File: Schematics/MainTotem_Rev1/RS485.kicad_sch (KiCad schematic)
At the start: 0 parts

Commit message: Added RS485 functionality to MainTotemLite
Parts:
- added C23, C25: 0.1u, symbol Device:C
- added C24: 10u, symbol Device:C
- added C27, C32: 100n, symbol Device:C
- added D1: SM712_SOT23, Package_TO_SOT_SMD:SOT-23, symbol Diode:SM712_SOT23
- added J1, J2: S6B-XH-A, S6B-XH-A:JST_S6B-XH-A, symbol TotemBusMale:S6B-XH-A
- added J3: Conn_02x05_Odd_Even, symbol Connector_Generic:Conn_02x05_Odd_Even
- added JP1: Jumper_2_Open, symbol Jumper:Jumper_2_Open
- added PROG: GREEN, symbol Device:LED
- added R1: 120, symbol Device:R
- added R10, R8, R9: 1k, symbol Device:R
- added R2, R3, R7: 10k, symbol Device:R
- added RS485: YELLOW, symbol Device:LED
- added U3: THVD1450D, D0008A_N, symbol RS485Transceiver:THVD1450D
- added U4: STM32G071KBT6, LQFP-32, symbol STM32G0:STM32G071KBT6
- added UH_OH: RED, symbol Device:LED
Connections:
- new net: R8.1, U4.11 (PA4)
- new net: R9.1, U4.12 (PA5)
- new net: R10.1, U4.13 (PA6)
- new net: U3.4 (D), U4.19 (PA9)
- new net: R2.2, U3.1 (R), U4.21 (PA10)
- new net: R3.1, U3.2 (RE_N), U3.3 (DE), U4.23 (PA12[PA10])
- new net: J3.2 (Pin_2), U4.24 (PA13)
- new net: J3.4 (Pin_4), R7.1, U4.25 (PA14-BOOT0)
- new net: C27.1, J3.10 (Pin_10), U4.6 (PF2-NRST)
- new net: D1.1 (A1), J1.2, J2.2, JP1.2 (B), U3.6 (A)
- new net: D1.2 (A2), J1.3, J2.3, R1.2, U3.7 (B)
- new net: PROG.2 (A), R10.2
- new net: R8.2, UH_OH.2 (A)
- new net: R9.2, RS485.2 (A)
- new net: JP1.1 (A), R1.1
- new net +3V3: C23.1, C24.1, C25.1, C32.1, J1.1, J2.1, J3.1 (Pin_1), J3.6 (Pin_6), R2.1, U3.8 (VCC), U4.4 (VDD)
- new net BUSH7BOOT0: U4.27 (PB3)
- new net BUSH7NRST: U4.17 (PB2)
- new net BUSH7SWCLK: U4.16 (PB1)
- new net BUSH7SWDIO: U4.15 (PB0)
- new net BUSH7UARTRX: U4.32 (PB8)
- new net BUSHH7UARTTX: U4.1 (PB9)
- new net G0UARTRX: J3.8 (Pin_8), U4.10 (PA3)
- new net G0UARTTX: J3.7 (Pin_7), U4.9 (PA2)
- new net GND: C23.2, C24.2, C25.2, C27.2, C32.2, D1.3 (common), J1.4, J2.4, J3.3 (Pin_3), J3.5 (Pin_5), J3.9 (Pin_9), PROG.1 (K), R3.2, R7.2, RS485.1 (K), U3.5 (GND), U3.9 (PAD), U4.5 (VSS), UH_OH.1 (K)
- no-connect marks 0 -> 17
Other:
- note added: "Configure these as Analog Mode pins to avoid unwated signal"
- note added: "Don't connect the 3V3 unless you are powering the ShamanLink and other modules with it. It will compete with the 3V3 on the other boards. Also, you probably can't power the ShamanLink with it anyways since the PowerMUX expects inputs not only outputs."
- note added: "Label this jumper to determine if this MTL module is the terminating module on the RS485 bus"
- note added: "SWCLK/BOOT0, pull high to program with UART"
- note added: "SWDIO"

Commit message: Adding the MTL Schematics in post editing
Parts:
- added C64: 0.1u, symbol Device:C
- added D4: BAT54SW_115, BAT54SW_115:SOT65P210X110-3N, symbol BAT54SW_115:BAT54SW_115
- added SW2: SW_Push, symbol Switch:SW_Push
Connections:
- net +3V3: no longer C23.1, J1.1, J2.1
- net BUSH7NRST: now also D4.3, SW2.1; no longer U4.17 (PB2)
- net GND: now also C64.2, SW2.2
- new net: D4.2, U4.17 (PB2)
- new net 3V3PROGRAMMER: C23.1, C64.1, J1.1, J2.1
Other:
- note added: "I mean, this should be fine. The diode's forward voltage is about .32 V at the currents I am expecting. Therefore, if the G0 pulls to 0.1V LOW and the diode adds .32V, .42V must be less than .3Vdd for the NRST to register VIL. If Vdd is 3.3V, this shouldn't be an issue I hope."
- note added: "Pin PB2 needs to be set to OUTPUT OPEN DRAIN such that it never attempts to drive the net high. It resets the H7 by driving low, but if not driving, the pull up 10k resistor pulls up the net for us. If the G0 tries to drive the net high while the reset button is being pressed, there will be a 0 impedence short the gnd i.e. vcc to gnd :( The current could break the G0 or the H7, bad day. I placed 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"
- note added: "SL can power additional modules if they are not connected to power in order to program them"
- note removed: "Don't connect the 3V3 unless you are powering the ShamanLink and other modules with it. It will compete with the 3V3 on the other boards. Also, you probably can't power the ShamanLink with it anyways since the PowerMUX expects inputs not only outputs."
- moved on the sheet: C24, C25

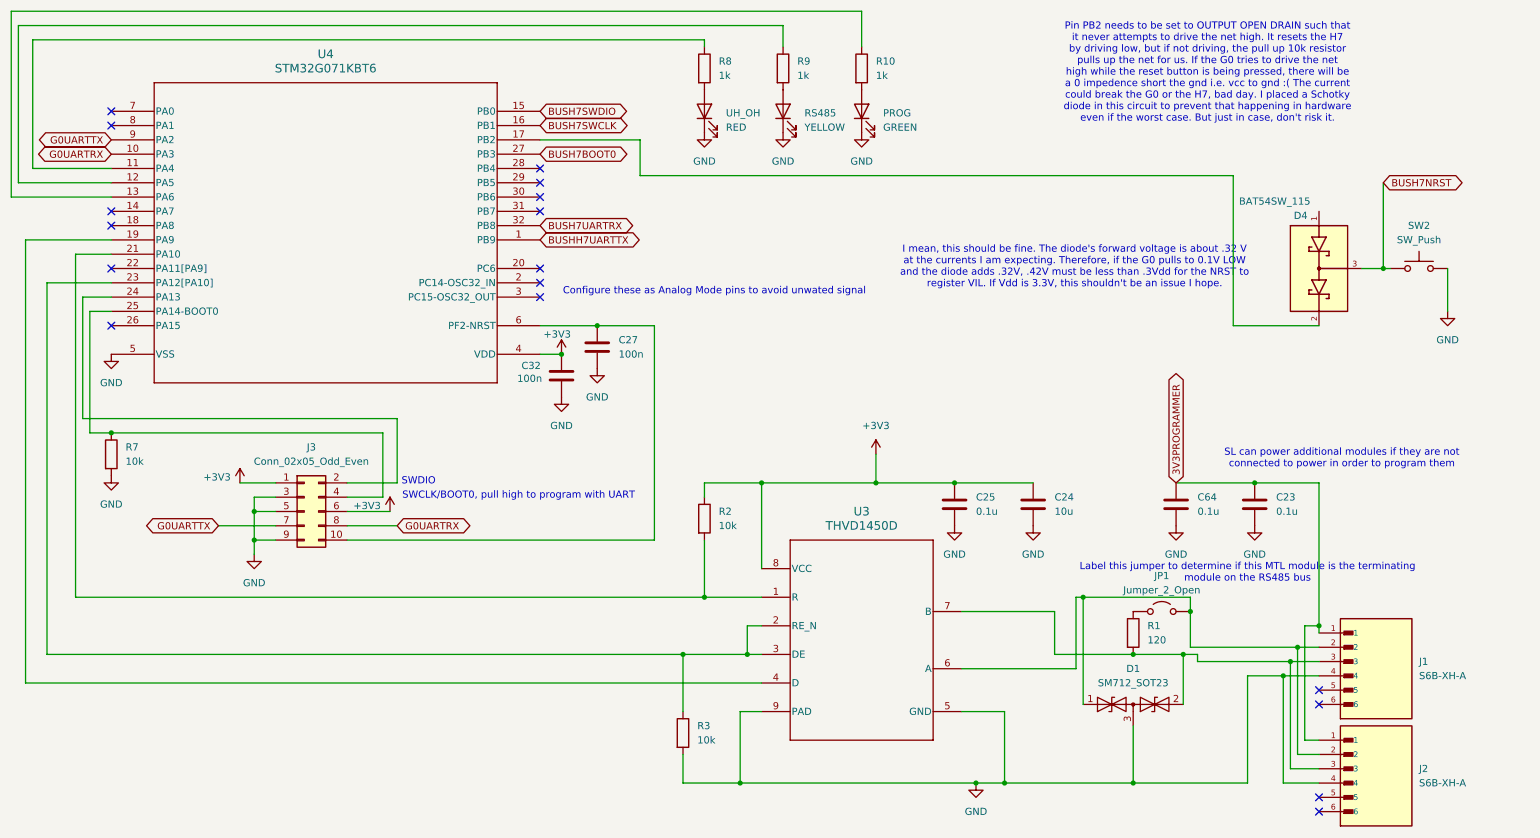
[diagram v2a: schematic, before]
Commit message: Layout Edits for Mezzanine Connector routing
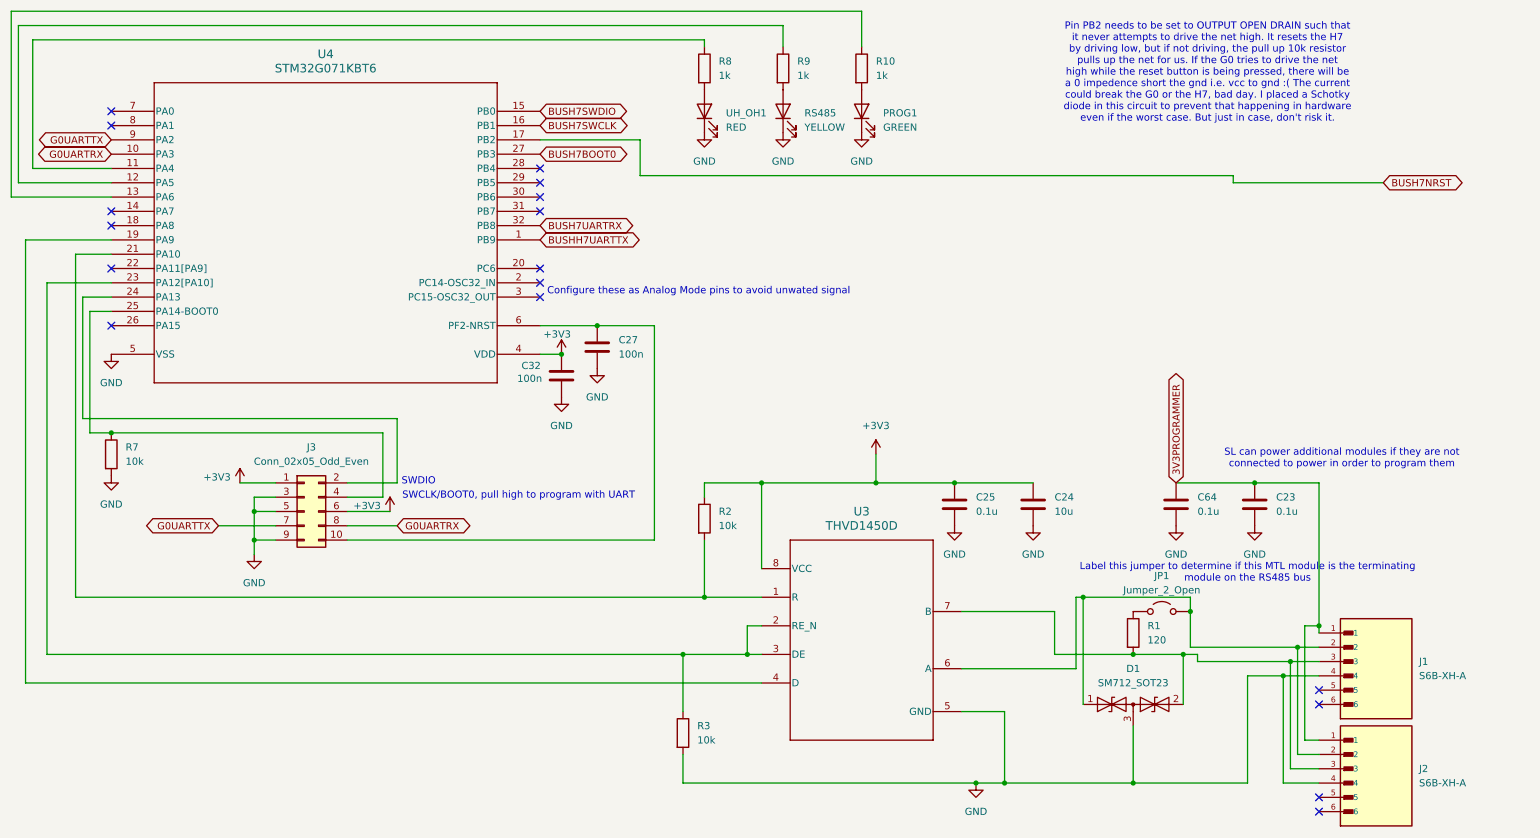
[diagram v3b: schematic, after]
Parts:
- removed D4: BAT54SW_115, BAT54SW_115:SOT65P210X110-3N, symbol BAT54SW_115:BAT54SW_115
- removed SW2: SW_Push, symbol Switch:SW_Push
- C23, C25, C27, C32, C64: footprint (none) -> Capacitor_SMD:C_0603_1608Metric_Pad1.08x0.95mm_HandSolder
- C24: footprint (none) -> Capacitor_SMD:C_0805_2012Metric_Pad1.18x1.45mm_HandSolder
- J1, J2: footprint S6B-XH-A:JST_S6B-XH-A -> JSTS6B-XH-A-1:JST_S6B-XH-A
- J3: footprint (none) -> Connector_PinHeader_2.54mm:PinHeader_2x05_P2.54mm_Vertical
- JP1: footprint (none) -> Connector_PinHeader_2.54mm:PinHeader_1x02_P2.54mm_Vertical
- PROG1: renamed from PROG; footprint (none) -> Resistor_SMD:R_0805_2012Metric_Pad1.20x1.40mm_HandSolder
- R1: footprint (none) -> Resistor_SMD:R_1210_3225Metric_Pad1.30x2.65mm_HandSolder
- R10, R2, R3, R7, R8, R9: footprint (none) -> Resistor_SMD:R_0603_1608Metric_Pad0.98x0.95mm_HandSolder
- RS485: footprint (none) -> Resistor_SMD:R_0805_2012Metric_Pad1.20x1.40mm_HandSolder
- U3: footprint D0008A_N -> RS485Transceiver:D0008A_M
- U4: footprint LQFP-32 -> STM32G0:LQFP-32-M
- UH_OH1: renamed from UH_OH; footprint (none) -> Resistor_SMD:R_0805_2012Metric_Pad1.20x1.40mm_HandSolder
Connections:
- net BUSH7NRST: now also U4.17 (PB2)
- net GND: no longer U3.9 (PAD)
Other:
- note removed: "I mean, this should be fine. The diode's forward voltage is about .32 V at the currents I am expecting. Therefore, if the G0 pulls to 0.1V LOW and the diode adds .32V, .42V must be less than .3Vdd for the NRST to register VIL. If Vdd is 3.3V, this shouldn't be an issue I hope."
